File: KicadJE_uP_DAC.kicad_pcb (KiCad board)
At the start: 2 copper layers, 100 x 100 mm, 214 parts, among them J201 CV1, J202 CV2, J203 OUT1, J204 OUT2, J205 IN1, J206 IN2, J301 AVR-ISP-6, J302 UART, J401 CV1, J402 CV2, J403 OUT1, J404 OUT2, J405 OUT3, J406 OUT4, J407 IN1, J408 IN2, J409 I2C, J501 BOOT, J502 UART, J503 USB_B_Micro, P201 Doepfer_Power_16pin, P401 Doepfer_Power_16pin, SW201 SW_SPDT, SW401 SW_SPDT, U201 TL072, U202 MCP4822, U203 TL072, U301 ATmega32A-AU, U401 TL072, U402 TL072, U403 TL072, U404 TL072, U405 MCP4822, U501 AMS1117-3.3, U502 STM32F103C8Tx, Y301 16MHz, Y501 8 MHz

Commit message: Sch cleanup and sorting of components in ATMega
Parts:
- removed the U201 at (170.9, 28.6)
- added D408: 1N1007, Diode_SMD:D_SOD-123, B.Cu at (126.9, 31.8)
- added D414: 1N1007, Diode_SMD:D_SOD-123, B.Cu at (126.9, 28.5)
- added D501: LED, LED_SMD:LED_0805_2012Metric_Pad1.15x1.40mm_HandSolder, B.Cu at (141.6, 32.0)
- added R501: 3k3, Resistor_SMD:R_0805_2012Metric_Pad1.15x1.40mm_HandSolder, B.Cu at (146.3, 32.0)
- C207, C210, C301, C302, C303, C304, C305, C306, C307, D301, J301, J302, R206, R209, R213, R220, R301, R302, R303, R304, R305, U202, U301, Y301: moved to B.Cu
- JP201: value JMP -> SS; moved to B.Cu
- JP202: value JMP -> MOSI; moved to B.Cu
- JP203: value JMP -> MISO; moved to B.Cu
- JP204: value JMP -> SCK; moved to B.Cu
- R502: renamed from R505; value 1k -> 2k2
- U201: renamed from U203; moved to B.Cu
- moved C305 136.0 mm to (194.6, 34.1), turned to 90 degrees
- moved C306 136.0 mm to (188.7, 34.1), turned to 90 degrees
- moved R305 136.0 mm to (191.6, 34.1), turned to 90 degrees
- moved R304 132.6 mm to (172.0, 32.5)
- moved C302 124.5 mm to (187.9, 39.9), turned to 90 degrees
- moved C307 124.5 mm to (185.0, 39.9), turned to 90 degrees
- moved J301 123.7 mm to (147.5, 42.5), turned to 0 degrees
- moved Y301 113.4 mm to (192.7, 45.4), turned to 90 degrees
- moved C304 110.0 mm to (178.2, 47.1), turned to 90 degrees
- moved C301 100.5 mm to (180.1, 51.9), turned to 90 degrees
- moved C303 100.5 mm to (177.2, 51.9), turned to 90 degrees
- moved R302 91.0 mm to (178.2, 56.6), turned to 90 degrees
- moved U301 91.0 mm to (188.8, 56.7), turned to 90 degrees
- moved R301 81.6 mm to (180.1, 61.4), turned to 90 degrees
- moved R303 81.6 mm to (177.2, 61.4), turned to 90 degrees
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- renumbered C404 to C403, C405 to C404, C406 to C405, C407 to C406, C408 to C407, C409 to C408, C410 to C409, C411 to C410, C412 to C411, C413 to C412, C414 to C413, C415 to C414, C416 to C415, C417 to C416, C403 to C417, D408 to D409, D409 to D410, D410 to D411, D411 to D412, D412 to D413, D413 to D415, D414 to D416, D415 to D417, D416 to D418, D417 to D419, D418 to D420, D419 to D421, D420 to D422, D501 to D502, R501 to R503, R502 to R504, R503 to R505, R504 to R506, R506 to R507, R507 to R508, R508 to R509, R509 to R510, R510 to R511, R511 to R512
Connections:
- net 18 renamed R0_18
- net 19 renamed R1_19
- net 20 renamed R2_20
- net 21 renamed R3_21
- net Net-(C209-Pad1) renamed /KicadJE_ATMega32A_DAC/2_out
- net Net-(JP201-Pad1) renamed /KicadJE_ATMega32A_DAC/SS
- net Net-(JP202-Pad1) renamed /KicadJE_ATMega32A_DAC/SDI
- net Net-(JP204-Pad1) renamed /KicadJE_ATMega32A_DAC/SCK
- net Net-(R211-Pad1) renamed /KicadJE_ATMega32A_DAC/2_inv
- net Net-(R214-Pad2) renamed /KicadJE_ATMega32A_DAC/2_noninv
- C201 pad 1: Net-(C201-Pad1) -> GND
- C201 pad 2: Net-(C201-Pad2) -> +12V
- C202 pad 2: (no net) -> +12V
- C204 pad 1: Net-(C201-Pad1) -> GND
- C204 pad 2: Net-(C204-Pad2) -> -12V
- C205 pad 2: (no net) -> -12V
- C206 pad 1: Net-(C206-Pad1) -> /KicadJE_ATMega32A_DAC/1_out
- C407 pad 2: DACA -> STM_DACA
- C413 pad 2: DACB -> STM_DACB
- C417 pad 1: GNDA -> +5V
- C417 pad 2: +5VA -> GND
- D205 pad 1: 22 -> C0_22
- D206 pad 1: 23 -> C1_23
- D207 pad 1: 0 -> C2_0
- D209 pad 1: (no net) -> C0_22
- D210 pad 1: (no net) -> C1_23
- D211 pad 1: (no net) -> C2_0
- D213 pad 1: (no net) -> C0_22
- D214 pad 1: (no net) -> C1_23
- D215 pad 1: (no net) -> C2_0
- D217 pad 1: (no net) -> C0_22
- D218 pad 1: (no net) -> C1_23
- D219 pad 1: (no net) -> C2_0
- R205 pad 1: Net-(R205-Pad1) -> /KicadJE_ATMega32A_DAC/1_inv
- R205 pad 2: Net-(C206-Pad1) -> /KicadJE_ATMega32A_DAC/1_out
- R206 pad 2: Net-(R205-Pad1) -> /KicadJE_ATMega32A_DAC/1_inv
- R207 pad 1: Net-(C206-Pad1) -> /KicadJE_ATMega32A_DAC/1_out
- R208 pad 2: Net-(R208-Pad2) -> /KicadJE_ATMega32A_DAC/1_noninv
- R210 pad 2: 0 -> C2_0
- R221 pad 2: 22 -> C0_22
- R222 pad 2: 23 -> C1_23
- U201 pad 1: (no net) -> /KicadJE_ATMega32A_DAC/1_out
- U201 pad 2: (no net) -> /KicadJE_ATMega32A_DAC/1_inv
- U201 pad 3: (no net) -> /KicadJE_ATMega32A_DAC/1_noninv
- U401 pad 4: (no net) -> -12V
- U401 pad 8: (no net) -> +12V
- U405 pad 1: +5VA -> +5V
- U405 pad 6: DACB -> STM_DACB
- U405 pad 8: DACA -> STM_DACA

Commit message: LED and Xtal
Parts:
- C202, C203, C204, C206, C208, C209, C211, C212, D201, D202, D203, D204, D208, D212, D216, D220, R201, R202, R203, R204, R205, R207, R208, R210, R211, R212, R214, R215, R216, R217, R218, R219, R221, R222: moved to B.Cu
- moved D219 116.3 mm to (114.0, 57.0), turned to 90 degrees
- moved C305 114.4 mm to (119.0, 120.0)
- moved C306 107.5 mm to (124.0, 120.0)
- moved D217 100.0 mm to (148.0, 57.0), turned to 90 degrees
- moved Y301 98.2 mm to (124.0, 115.5), turned to 180 degrees
- moved D215 94.0 mm to (114.0, 121.0), turned to 90 degrees
- moved D211 89.9 mm to (114.0, 131.0), turned to 90 degrees
- moved D207 87.4 mm to (114.0, 142.0), turned to 90 degrees
- moved D218 84.2 mm to (130.0, 111.0), turned to 90 degrees
- moved U301 84.1 mm to (120.0, 105.0)
- moved D214 78.1 mm to (130.0, 121.0), turned to 90 degrees
- moved D210 73.2 mm to (130.0, 131.0), turned to 90 degrees
- moved D206 70.1 mm to (130.0, 142.0), turned to 90 degrees
- moved J302 65.3 mm to (138.5, 101.0), turned to 180 degrees
- moved C203 61.2 mm to (207.2, 72.1), turned to 90 degrees
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
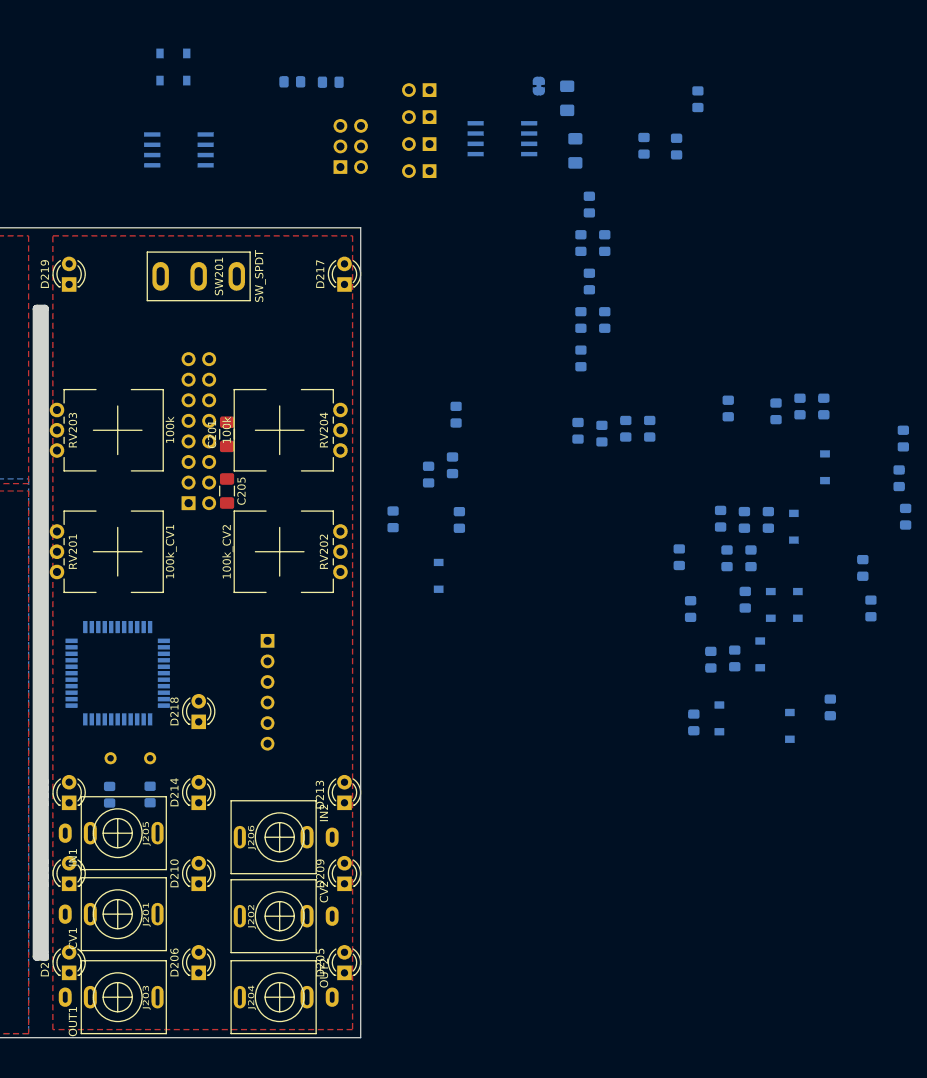
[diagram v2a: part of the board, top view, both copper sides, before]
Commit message: ATMega 32 placed again - decoupling added
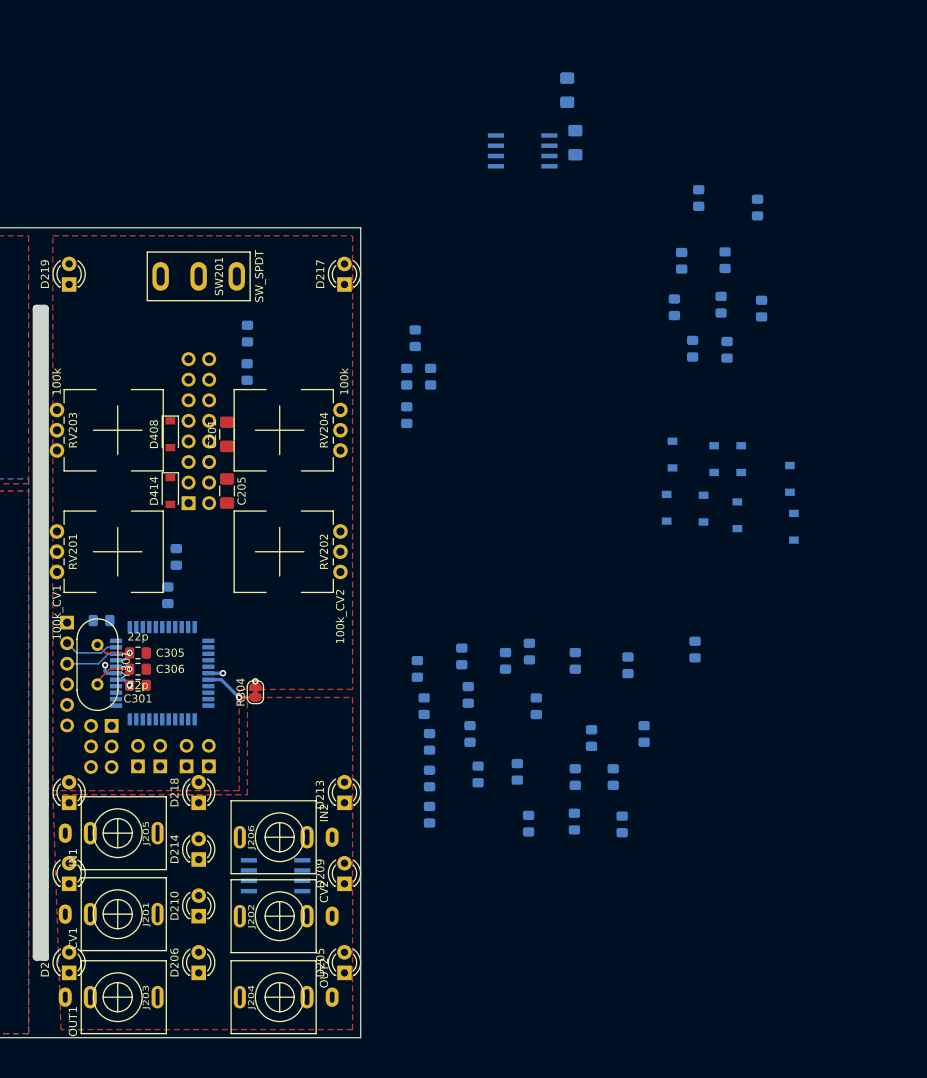
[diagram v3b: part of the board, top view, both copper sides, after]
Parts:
- C301, C305, C306, D408, D414, R304, Y301: moved to F.Cu
- moved JP204 90.9 mm to (122.5, 116.5), turned to 0 degrees
- moved U201 90.4 mm to (139.5, 130.0), turned to 180 degrees
- moved C307 89.0 mm to (118.0, 98.5), turned to 180 degrees
- moved JP201 84.7 mm to (131.2, 116.5), turned to 0 degrees
- moved R304 82.6 mm to (137.0, 107.3), turned to 90 degrees
- moved JP202 82.5 mm to (128.5, 116.5), turned to 0 degrees
- moved JP203 80.7 mm to (125.2, 116.5), turned to 0 degrees
- moved C301 79.4 mm to (122.5, 106.5), turned to 180 degrees
- moved J301 74.6 mm to (119.2, 111.5), turned to 180 degrees
- moved R305 71.0 mm to (176.5, 103.5)
- moved C303 67.0 mm to (126.2, 95.4)
- moved C304 67.0 mm to (127.2, 90.6)
- moved C204 59.2 mm to (199.0, 47.5)
- moved R210 58.3 mm to (162.5, 102.9)
- moved R219 58.3 mm to (163.3, 107.7)
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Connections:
- C301 pad 1: Net-(C301-Pad1) -> GND
- C303 pad 1: (no net) -> GND
- D201 pad 2: Net-(D201-Pad2) -> CV1
- D202 pad 1: Net-(D201-Pad2) -> CV1
- D203 pad 2: Net-(D203-Pad2) -> CV2
- D204 pad 1: Net-(D203-Pad2) -> CV2
- D208 pad 2: Net-(D208-Pad2) -> IN1
- D212 pad 1: Net-(D208-Pad2) -> IN1
- D216 pad 2: Net-(D216-Pad2) -> IN2
- D220 pad 1: Net-(D216-Pad2) -> IN2
- R304 pad 2: Net-(C301-Pad1) -> GND
- Y301 pad 1: (no net) -> Net-(C305-Pad1)
- Y301 pad 2: (no net) -> Net-(C306-Pad1)
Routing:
- net 32_9_Tx: track 0.00 -> 6.84 mm
- net Net-(C306-Pad1): track 0.00 -> 6.78 mm, vias 0 -> 1
- net GNDA: track 0.00 -> 6.71 mm, vias 0 -> 1
- net 32_8_Rx: track 0.00 -> 6.56 mm
- net Net-(C305-Pad1): track 0.00 -> 6.54 mm, vias 0 -> 2
- net GND: track 0.00 -> 4.73 mm, vias 0 -> 3
- net +5V: track 0.00 -> 1.96 mm, vias 0 -> 1

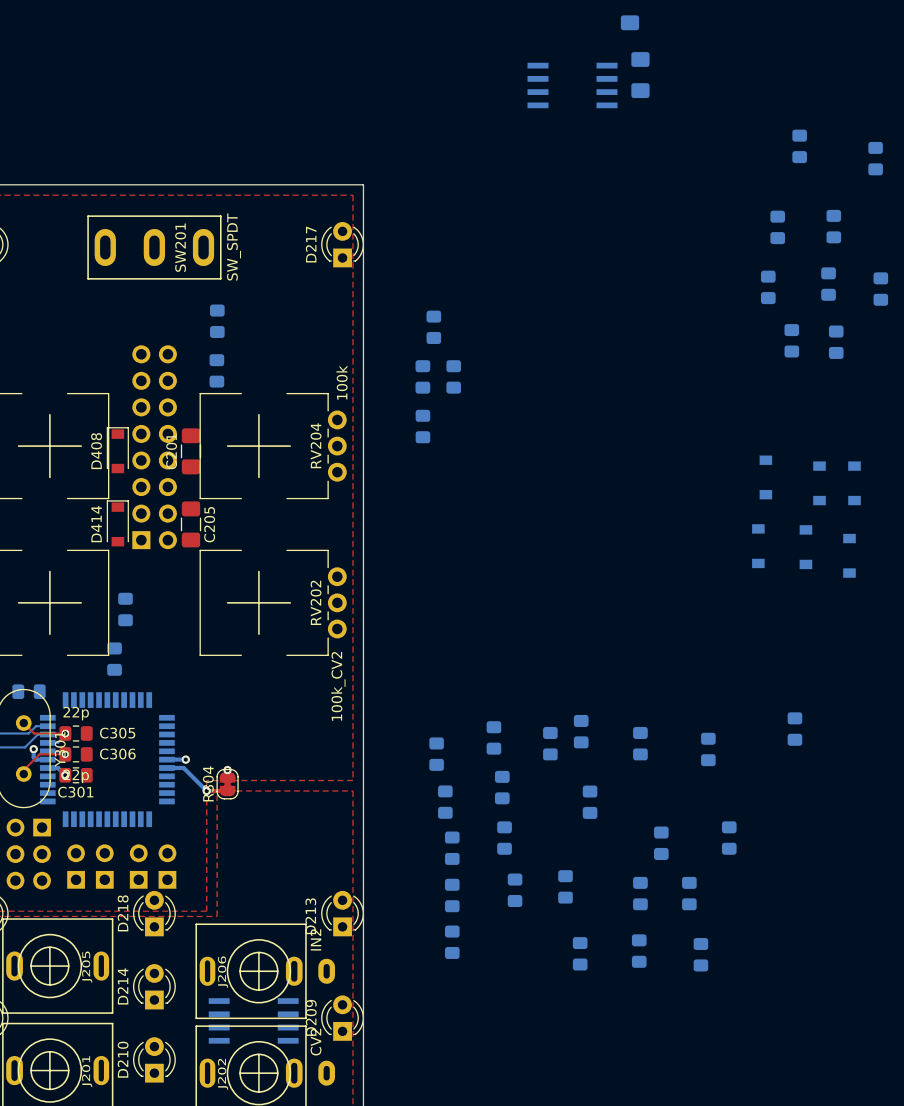
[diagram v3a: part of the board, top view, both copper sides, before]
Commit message: +5V ATMega
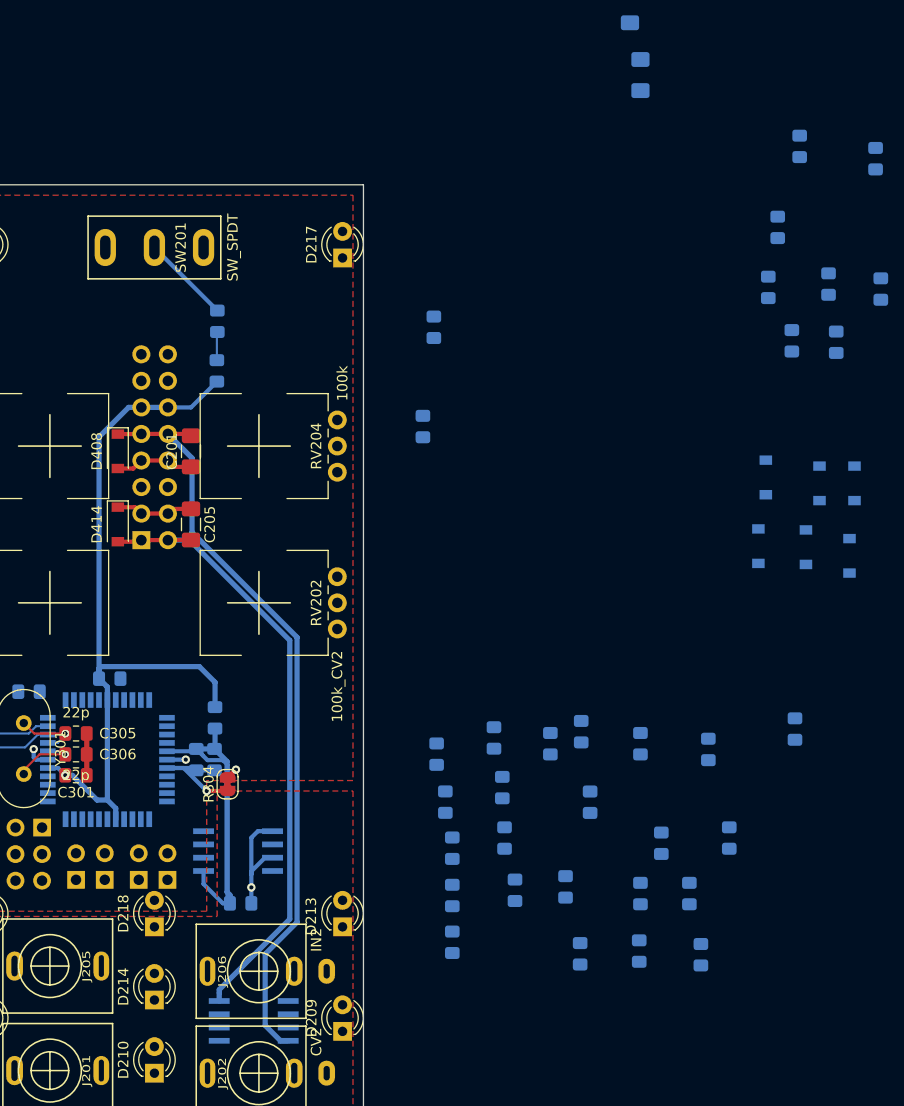
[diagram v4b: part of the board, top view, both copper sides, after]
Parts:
- moved C203 86.1 mm to (138.2, 118.8), turned to 180 degrees
- moved U202 79.9 mm to (138.0, 113.8)
- moved R303 41.7 mm to (135.8, 105.0), turned to 270 degrees
- moved R301 39.8 mm to (135.8, 101.0)
- moved C304 15.9 mm to (134.0, 105.0)
- moved C303 1.92 mm to (125.7, 97.2), turned to 180 degrees
- turned U201 to 0 degrees
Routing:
- net +12V: track 0.00 -> 72.9 mm
- net +5V: track 1.96 -> 72.8 mm
- net -12V: track 0.00 -> 60.0 mm
- net +5VA: track 0.00 -> 43.5 mm
- net GND: track 4.73 -> 32.7 mm
- net GNDA: track 6.71 -> 22.8 mm, vias 1 -> 2
- net Net-(D501-Pad2): track 0.00 -> 2.71 mm

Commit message: 12V PWR
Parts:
- moved C204 107.1 mm to (137.2, 135.0), turned to 270 degrees
- moved C209 104.6 mm to (144.8, 139.8)
- moved C206 102.0 mm to (133.2, 141.0)
- moved C202 94.4 mm to (141.0, 135.0), turned to 270 degrees
- moved C207 90.2 mm to (138.2, 121.2), turned to 0 degrees
- moved C208 88.7 mm to (135.2, 130.6), turned to 270 degrees
- moved C210 84.7 mm to (145.0, 112.0), turned to 180 degrees
- moved C211 83.7 mm to (143.2, 130.6), turned to 270 degrees
- moved R209 47.4 mm to (133.2, 126.8), turned to 270 degrees
- moved R215 41.2 mm to (141.2, 126.8), turned to 270 degrees
- moved R208 26.6 mm to (133.2, 130.6), turned to 270 degrees
- moved R202 23.6 mm to (167.5, 127.1)
- moved R207 23.6 mm to (168.9, 140.8)
- moved R211 23.6 mm to (170.3, 147.2)
- moved R212 23.6 mm to (171.3, 132.7)
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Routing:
- net +12V: track 72.9 -> 87.1 mm
- net -12V: track 60.0 -> 73.7 mm

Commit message: Routed
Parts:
- removed JP203: MISO, Connector_PinSocket_2.54mm:PinSocket_1x02_P2.54mm_Vertical
- D301, R210, R216, R217, R219, R220, R221, R222, R302: moved to F.Cu
- moved D212 94.2 mm to (118.5, 127.5), turned to 270 degrees
- moved C302 91.1 mm to (125.2, 112.8), turned to 0 degrees
- moved D208 87.1 mm to (118.5, 122.6), turned to 270 degrees
- moved D202 81.7 mm to (115.4, 83.4), turned to 180 degrees
- moved C212 80.7 mm to (117.6, 98.4)
- moved D201 77.0 mm to (115.4, 81.2), turned to 0 degrees
- moved R305 65.2 mm to (115.8, 108.2)
- moved R201 65.2 mm to (116.0, 90.0), turned to 0 degrees
- moved R205 63.2 mm to (137.4, 147.0), turned to 180 degrees
- moved R203 60.1 mm to (121.8, 124.6), turned to 180 degrees
- moved D204 57.7 mm to (145.5, 85.2), turned to 0 degrees
- moved R220 57.5 mm to (134.8, 99.8), turned to 0 degrees
- moved R222 54.5 mm to (134.8, 103.8), turned to 0 degrees
- moved R302 54.4 mm to (126.2, 108.8), turned to 180 degrees
- moved D216 53.5 mm to (139.9, 100.4), turned to 270 degrees
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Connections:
- C202 pad 1: GND -> GNDA
- C204 pad 1: GND -> GNDA
- C302 pad 2: (no net) -> +5V
- D202 pad 2: GNDA -> GND
- D204 pad 2: GNDA -> GND
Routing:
- net +5V: track 72.8 -> 201.2 mm, vias 1 -> 4
- net C2_0: track 0.00 -> 119.1 mm, vias 0 -> 8
- net R3_21: track 0.00 -> 117.7 mm, vias 0 -> 9
- net R0_18: track 0.00 -> 113.0 mm, vias 0 -> 5
- net C0_22: track 0.00 -> 104.2 mm, vias 0 -> 5
- net R1_19: track 0.00 -> 86.7 mm, vias 0 -> 6
- net R2_20: track 0.00 -> 80.3 mm, vias 0 -> 5
- net 32_2_INT2: track 0.00 -> 76.4 mm, vias 0 -> 2
- net Net-(J201-PadTN): track 0.00 -> 61.5 mm, vias 0 -> 2
- net 32_1: track 0.00 -> 60.0 mm, vias 0 -> 2
- net Net-(J201-PadT): track 0.00 -> 56.7 mm
- net Duty: track 0.00 -> 51.4 mm, vias 0 -> 2
- net Wave: track 0.00 -> 49.8 mm, vias 0 -> 3
- net C1_23: track 0.00 -> 46.8 mm, vias 0 -> 6
- net CV2: track 0.00 -> 40.2 mm, vias 0 -> 2
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
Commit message: Primary components
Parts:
- removed the U401 at (-22.6, 2.63)
- removed the U402 at (-22.6, 10.4)
- added JP406: PWM_1, Connector_PinSocket_2.54mm:PinSocket_1x02_P2.54mm_Vertical, B.Cu at (43.1, 114.9)
- added JP407: PWM_2, Connector_PinSocket_2.54mm:PinSocket_1x02_P2.54mm_Vertical, B.Cu at (46.9, 114.9)
- C402, C403, C405, C406, C407, C408, C409, C410, C411, C412, C413, C414, C415, C416, C417, C501, C502, C503, C504, C505, C506, C507, D404, D409, D413, D418, D419, D420, D421, D422, D502, J501, J502, J503, P401, R401, R402, R403, R404, R405, R406, R407, R408, R409, R410, R411, R412, R413, R414, R415, R416, R417, R418, R419, R420, R421, R422, R423, R424, R425, R426, R427, R428, R502, R503, R504, R505, R506, R507, R508, R509, R510, R511, R512, U405, U501, U502, Y501: moved to B.Cu
- JP403: value JMP -> CS; moved to B.Cu
- JP404: value JMP -> SCK; moved to B.Cu
- JP405: value JMP -> SDI; moved to B.Cu
- RV401: value 100k -> 100k CV1
- RV402: value 100k -> 100k Wave
- RV403: value 100k -> 100k Duty
- RV404: value 100k -> 100k CV2
- U401: renamed from U403; moved to B.Cu
- U402: renamed from U404; moved to B.Cu
- moved C504 136.4 mm to (75.6, 100.6), turned to 270 degrees
- moved C505 131.6 mm to (65.7, 102.8)
- moved C503 130.8 mm to (73.3, 90.7), turned to 0 degrees
- moved J503 130.8 mm to (84.7, 103.0), turned to 270 degrees
- moved C506 128.3 mm to (63.1, 95.8), turned to 90 degrees
- moved J404 127.6 mm to (78.8, 135.0), turned to 90 degrees
- moved U405 127.6 mm to (69.5, 108.8)
- moved J403 125.5 mm to (60.0, 145.0), turned to 270 degrees
- moved R510 125.1 mm to (-1.28, 140.7)
- moved R511 125.1 mm to (3.47, 140.7)
- moved U501 124.0 mm to (78.8, 60.0), turned to 0 degrees
- moved R505 123.5 mm to (31.2, 139.8)
- moved R502 123.1 mm to (10.5, 146.3)
- moved C413 120.6 mm to (38.7, 115.6)
- moved J406 120.5 mm to (78.8, 145.0), turned to 90 degrees
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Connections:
- C402 pad 1: GND -> GNDA
- C403 pad 1: GND -> GNDA
- U401 pad 1: (no net) -> Net-(C405-Pad1)
- U401 pad 2: (no net) -> Net-(R403-Pad2)
- U401 pad 3: (no net) -> Net-(R410-Pad2)
- U401 pad 4: (no net) -> -12V
- U401 pad 8: (no net) -> +12V
- U402 pad 1: (no net) -> Net-(C406-Pad1)
- U402 pad 2: (no net) -> Net-(R405-Pad2)
- U402 pad 3: (no net) -> Net-(R412-Pad2)
- U402 pad 4: (no net) -> -12V
- U402 pad 8: (no net) -> +12V
- U502 pad 45: (no net) -> /KicadJE_STM32F0/STM32F103C8/STM32_SCL1_PWM_PB8
- U502 pad 46: (no net) -> /KicadJE_STM32F0/STM32F103C8/STM32_SDA1_PWM_PB9
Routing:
- net C2_0: track 119.1 -> 119.6 mm
